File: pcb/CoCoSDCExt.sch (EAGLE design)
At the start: 49 parts, among them IC1 AM29F040J, IC10 YAC512-M, IC14 TL974, IC15 TL974, IC2 XC9572XLVQG64, IC3 AS6C4008SIN, IC9 YMF262-M, X1 EXPANSION_PORT_COCO, X2 EXPANSION_PORT_COCOS

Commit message: fully routed
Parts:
- added C3.1: .1, resistor:C-USC0402
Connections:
- removed net !IRQ_AUDIO: IC9A.!IRQ
- removed net !OE: IC9A.!RD
- removed net AB0: IC9A.A0
- removed net AB1: IC9A.A1
- net !CE_RAM: now also IC2.FB4MC11; no longer IC2.FB4MC4
- net !CE_YMF262: now also IC2.FB3MC14
- net !CTS: now also IC2.FB1MC15; no longer IC2.FB1MC17
- net !NMI: now also IC9A.!IRQ
- net !RESET: now also IC2.FB1MC10-I/O/GCK2; no longer IC2.FB2MC12
- net !RESET_AUDIO: now also IC2.FB4MC5
- net !SCS: now also IC2.FB3MC8; no longer IC2.FB1MC12
- net !SLENB: now also IC2.FB3MC3; no longer IC2.FB3MC8
- net +5V: now also C3.1.1
- net A0: now also IC2.FB2MC12, IC9A.A0; no longer IC2.FB2MC14-I/O/GTS1
- net A1: now also IC9A.A1
- net A14: now also IC2.FB3MC9; no longer IC2.FB3MC5
- net A15: now also IC2.FB3MC4; no longer IC2.FB3MC9
- net BA15: now also IC2.FB4MC3; no longer IC2.FB1MC15
- net BA16: now also IC2.FB4MC8; no longer IC2.FB3MC2
- net BA18: now also IC2.FB4MC4; no longer IC2.FB4MC11
- net DB0: now also IC2.FB3MC5
- net DB1: now also IC2.FB1MC12
- net DB2: now also IC2.FB1MC17
- net DB3: now also IC2.FB3MC2
- net DB4: now also IC2.FB3MC11
- net DB5: now also IC2.FB3MC6
- net DB6: now also IC2.FB3MC15
- net DB7: now also IC2.FB3MC17
- net GND: now also C3.1.2, IC9A.!RD
- net R/!W: now also IC2.FB2MC14-I/O/GTS1; no longer IC2.FB1MC10-I/O/GCK2

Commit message: Added SN76489AN
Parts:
- removed OSC1: 16MHz, crystal:ASE
- added C1, C2: 1u, cap-pan40:C-BP-SMD-SV-B
- added C4.1: .1, rcl:C-USC0402
- added C5.1, C6.1: .1, resistor:C-USC0402
- added IC4: SN76489R, texas-instruments:SN76489R
- added IC5, IC6: 16MHz, crystal:ASE
- added R1: 2K, resistor:R-US_R1206
- added R2: 10K, resistor:R-US_R1206
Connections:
- new net !CE_SN: IC2.FB3MC16, IC4A.!CE
- new net !WE_AUDIO: IC2.FB3MC10, IC4A.!WE, IC9A.!WR
- new net CN_CH_0: IC4A.AUDIO
- new net N$1: IC4A.CLOCK, IC6.OUT
- new net N$2: C1.2, C2.2, R1.1
- new net N$3: C2.1, R2.2
- new net READY: IC2.FB3MC12, IC4A.READY
- new net SN_CH_0: R1.2
- net !WE: no longer IC9A.!WR
- net +3V3: now also C5.1.1, C6.1.1, IC5.VDD, IC6.VDD; no longer OSC1.VDD
- net +5V: now also C4.1.1, IC4P.VCC
- net AUDIO_R: now also C1.1
- net DB0: now also IC4A.D0
- net DB1: now also IC4A.D1
- net DB2: now also IC4A.D2
- net DB3: now also IC4A.D3
- net DB4: now also IC4A.D4
- net DB5: now also IC4A.D5
- net DB6: now also IC4A.D6
- net DB7: now also IC4A.D7
- net GND: now also C4.1.2, C5.1.2, C6.1.2, IC4P.GND, IC5.GND, IC6.GND; no longer OSC1.GND
- net N$12: now also IC5.OUT; no longer OSC1.OUT
- net N$17: now also R2.1

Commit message: More fixes
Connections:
- removed net CN_CH_0: IC4A.AUDIO
- new net N$4: IC2.FB4MC2
- net SN_CH_0: now also IC4A.AUDIO
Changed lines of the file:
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@@
 <wire x1="383.54" y1="127" x2="370.84" y2="127" width="0.1524" layer="91"/>
 <pinref part="IC2" gate="G$1" pin="FB4MC4"/>
-<wire x1="360.68" y1="127" x2="370.84" y2="127" width="0.1524" layer="91"/>
 </segment>
 </net>
@@
 <wire x1="370.84" y1="86.36" x2="388.62" y2="86.36" width="0.1524" layer="91"/>
 <label x="388.62" y="86.36" size="1.27" layer="95" xref="yes"/>
+</segment>
+</net>
+<net name="N$4" class="0">
+<segment>
+<pinref part="IC2" gate="G$1" pin="FB4MC2"/>
+<wire x1="370.84" y1="106.68" x2="414.02" y2="106.68" width="0.1524" layer="91"/>
 </segment>
 </net>
@@
 </segment>
 </net>
-<net name="CN_CH_0" class="0">
-<segment>
-<pinref part="IC4" gate="A" pin="AUDIO"/>
-<wire x1="101.6" y1="119.38" x2="104.14" y2="119.38" width="0.1524" layer="91"/>
-<label x="104.14" y="119.38" size="1.27" layer="95" xref="yes"/>
-</segment>
-</net>
 <net name="N$2" class="0">
 <segment>
@@
 <wire x1="147.32" y1="50.8" x2="144.78" y2="50.8" width="0.1524" layer="91"/>
 <label x="144.78" y="50.8" size="1.27" layer="95" rot="R180" xref="yes"/>
+</segment>
+<segment>
+<pinref part="IC4" gate="A" pin="AUDIO"/>
+<wire x1="101.6" y1="119.38" x2="104.14" y2="119.38" width="0.1524" layer="91"/>
+<label x="104.14" y="119.38" size="1.27" layer="95" xref="yes"/>
 </segment>
 </net>
@@
 </sheet>
 </sheets>
+<errors>
+</errors>
 </schematic>
 </drawing>

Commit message: Fixed SN signalling
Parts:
- added IC7: 74AHC1G08DCK, 74xx-little-us:74AHC1G08DCK
- added JP2: (no value), jumper-jlb:JP1Q
- added R3, R4: 10K, resistor:R-US_R0402
- added R5: 2K2, resistor:R-US_R0402
- added SJ1: (no value), jumper:SJ
- IC5: value 16MHz -> 14.318MHz
- IC6: value 16MHz -> 4MHz
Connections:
- removed net !WE_AUDIO: IC2.FB3MC10, IC4A.!WE, IC9A.!WR
- new net !CE_SN': IC4A.!CE, IC7A.O
- new net !CTS': IC2.FB4MC5, X2X.!CTS
- new net N$5: IC2.FB3MC12, R4.2, SJ1.2
- net !CE_SN: now also IC7A.I1; no longer IC4A.!CE
- net !CE_YMF262: now also IC2.FB3MC15; no longer IC2.FB3MC14
- net !CTS: no longer X2X.!CTS
- net !RESET_AUDIO: now also IC2.FB4MC2; no longer IC2.FB4MC5
- net !WE: now also IC9A.!WR
- net +3V3: now also R3.1, R4.1
- net +5V: now also IC7P.VCC, R5.1
- net DB0: now also IC2.FB3MC11; no longer IC2.FB3MC5
- net DB1: now also IC2.FB3MC5; no longer IC2.FB1MC12
- net DB2: now also IC2.FB3MC2; no longer IC2.FB1MC17
- net DB3: now also IC2.FB1MC12; no longer IC2.FB3MC2
- net DB4: now also IC2.FB3MC6; no longer IC2.FB3MC11
- net DB5: now also IC2.FB3MC14; no longer IC2.FB3MC6
- net DB6: now also IC2.FB3MC17; no longer IC2.FB3MC15
- net DB7: now also IC2.FB3MC10; no longer IC2.FB3MC17
- net GND: now also IC7P.GND, JP2.1, SJ1.1
- net N$4: now also IC2.FB1MC17, JP2.2, R3.2; no longer IC2.FB4MC2
- net READY: now also IC4A.!WE, IC7A.I0, R5.2; no longer IC2.FB3MC12
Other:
- moved on the sheet: 3V3, C2.1, C2.2, C2.3, C2.4, C8, C9, GND, IC2, TCK, TDI, TDO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

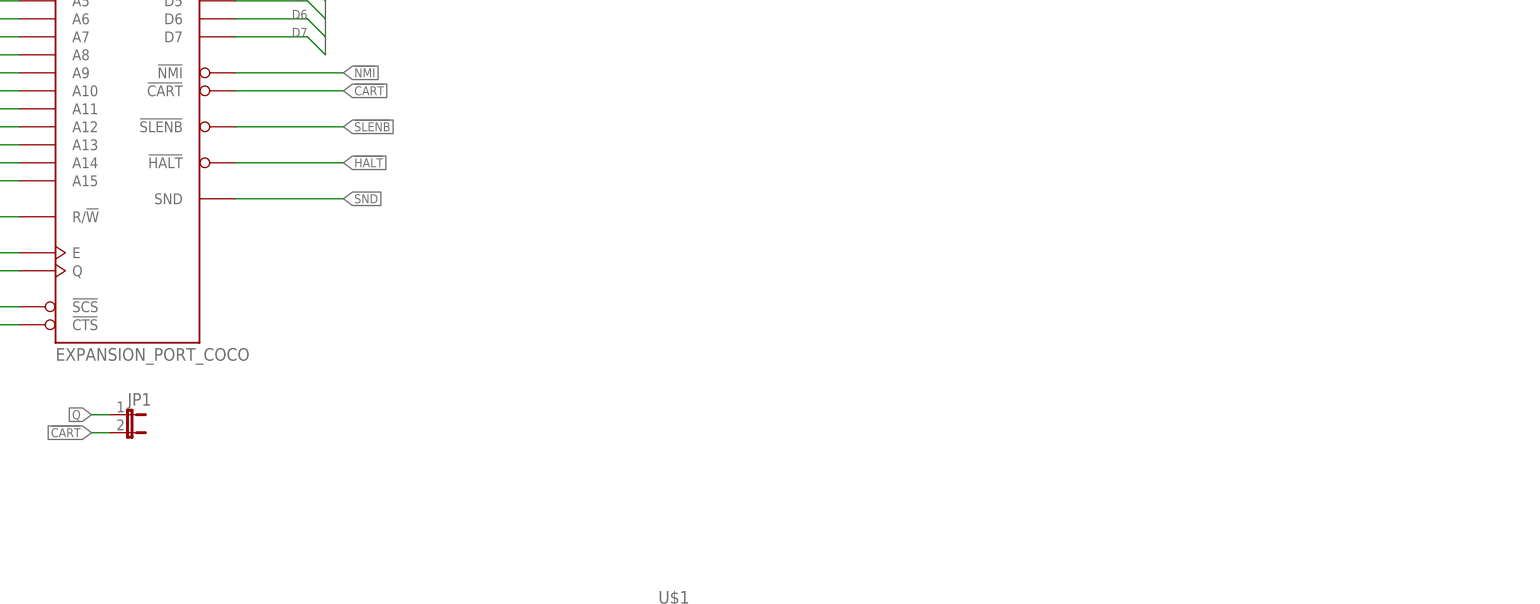
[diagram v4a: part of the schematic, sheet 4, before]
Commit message: Optimized SN signalling and reduced parts count
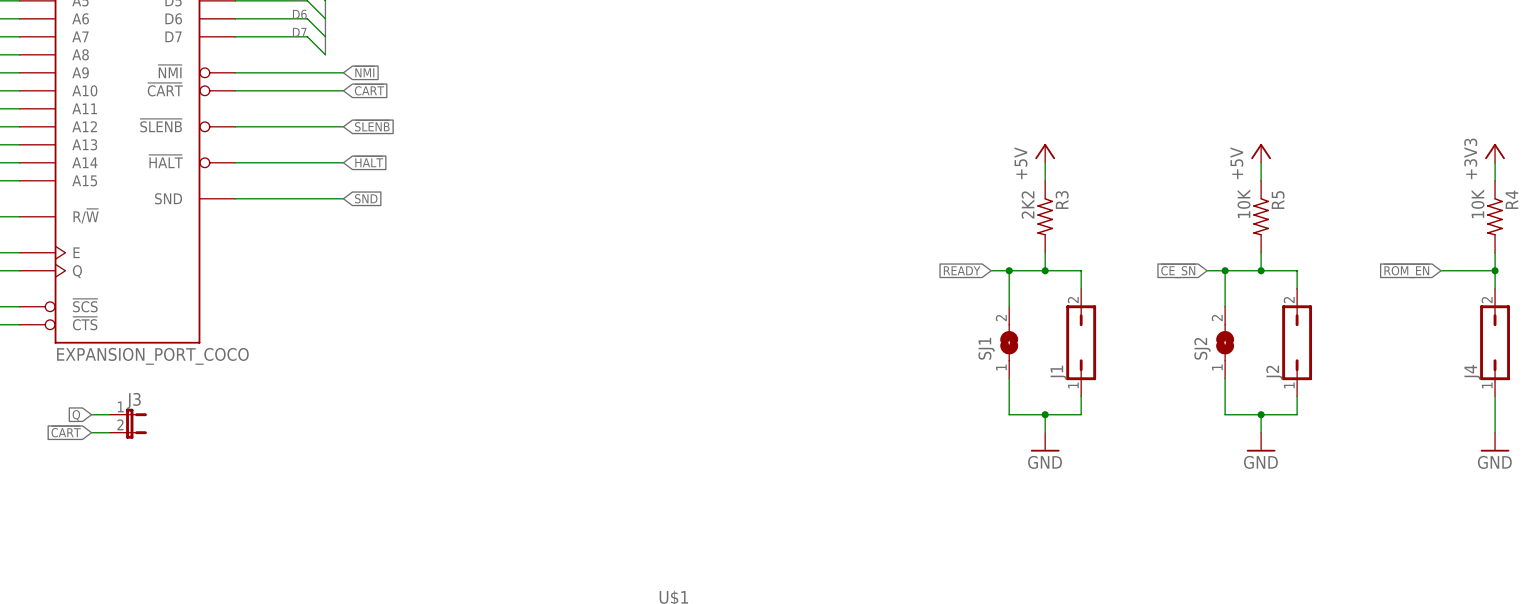
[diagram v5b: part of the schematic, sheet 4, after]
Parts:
- removed IC7: 74AHC1G08DCK, 74xx-little-us:74AHC1G08DCK
- removed JP2: (no value), jumper-jlb:JP1Q
- added J1, J2, J4: (no value), jumper-jlb:JP1Q
- added SJ2: (no value), jumper:SJ
- R3: value 10K -> 2K2
- R5: value 2K2 -> 10K
- renumbered JP1 to J3
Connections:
- removed net !CE_SN': IC4A.!CE, IC7A.O
- removed net N$4: IC2.FB1MC17, JP2.2, R3.2
- removed net N$5: IC2.FB3MC12, R4.2, SJ1.2
- new net !ROM_EN: IC2.FB1MC17, J4.2, R4.2
- net !CART: now also IC9A.!IRQ
- net !CE_SN: now also IC2.FB3MC12, IC4A.!CE, J2.2, R5.2, SJ2.2; no longer IC2.FB3MC16, IC7A.I1
- net !NMI: no longer IC9A.!IRQ
- net +3V3: no longer R3.1
- net +5V: now also R3.1; no longer IC7P.VCC
- net GND: now also J1.1, J2.1, J4.1, SJ2.1; no longer IC7P.GND, JP2.1
- net READY: now also IC2.FB3MC16, J1.2, R3.2, SJ1.2; no longer IC7A.I0, R5.2
